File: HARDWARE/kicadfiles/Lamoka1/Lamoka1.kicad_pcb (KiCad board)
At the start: 2 copper layers, 48 parts, among them J1 Boostconverteroutput, J2 Boostconverterinput, J3 Groundconnection, Q1 CSD19531Q5A, Q2 CSD19531Q5A, Q3 CSD19531Q5A, Q4 CSD19531Q5A, U2 LM5122QMHE/NOPB, U3 LM5122QMHE/NOPB

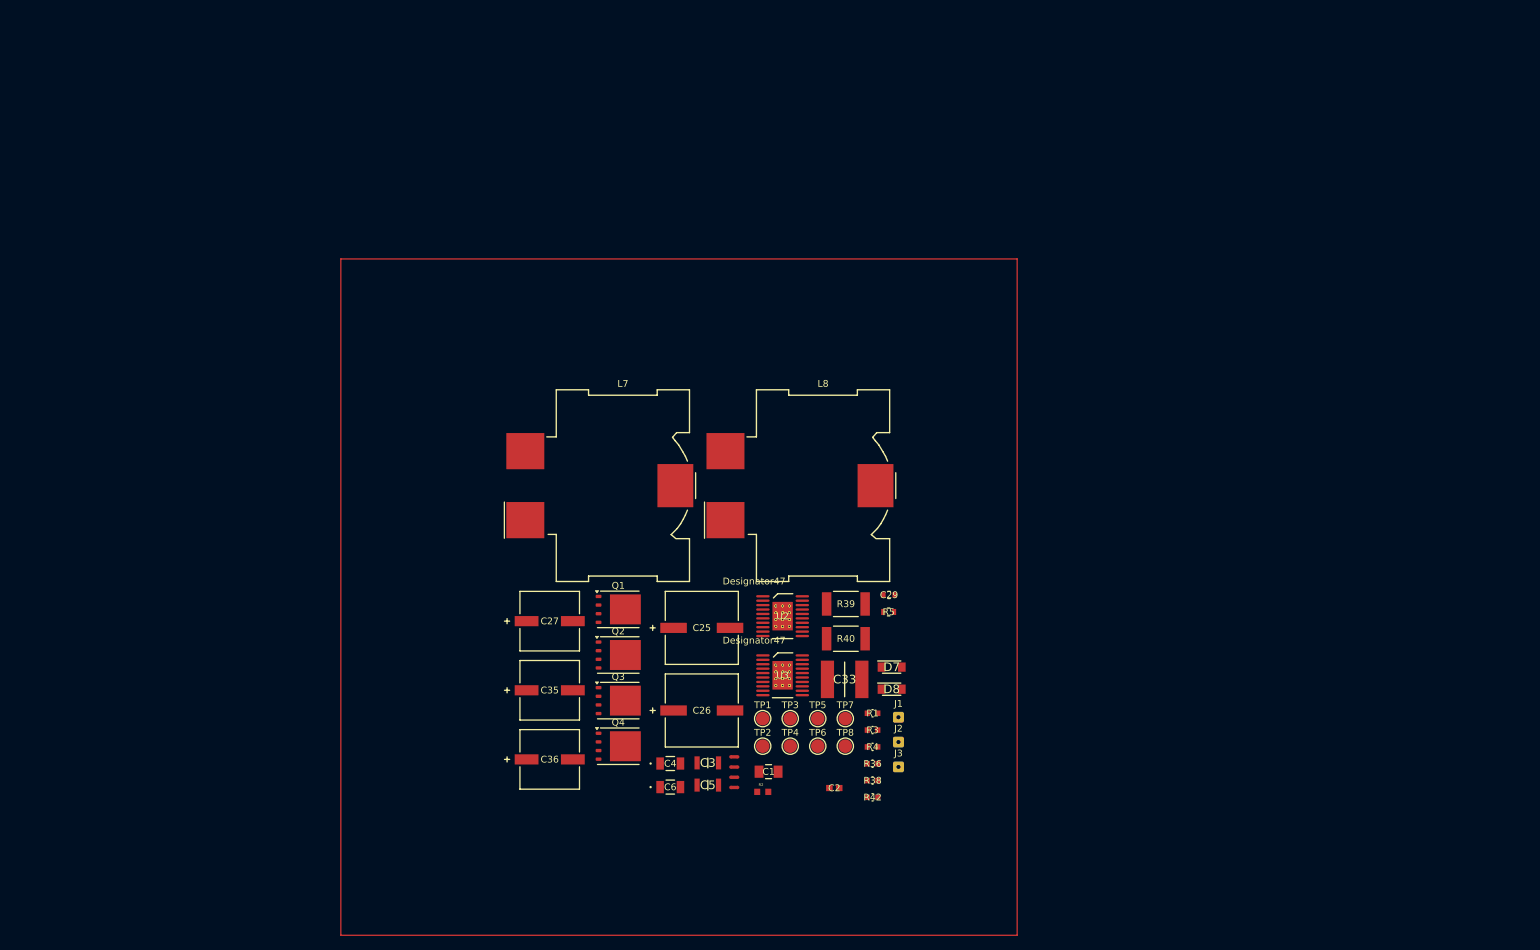
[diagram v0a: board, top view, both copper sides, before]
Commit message: Take things out so boost converter can be standalone
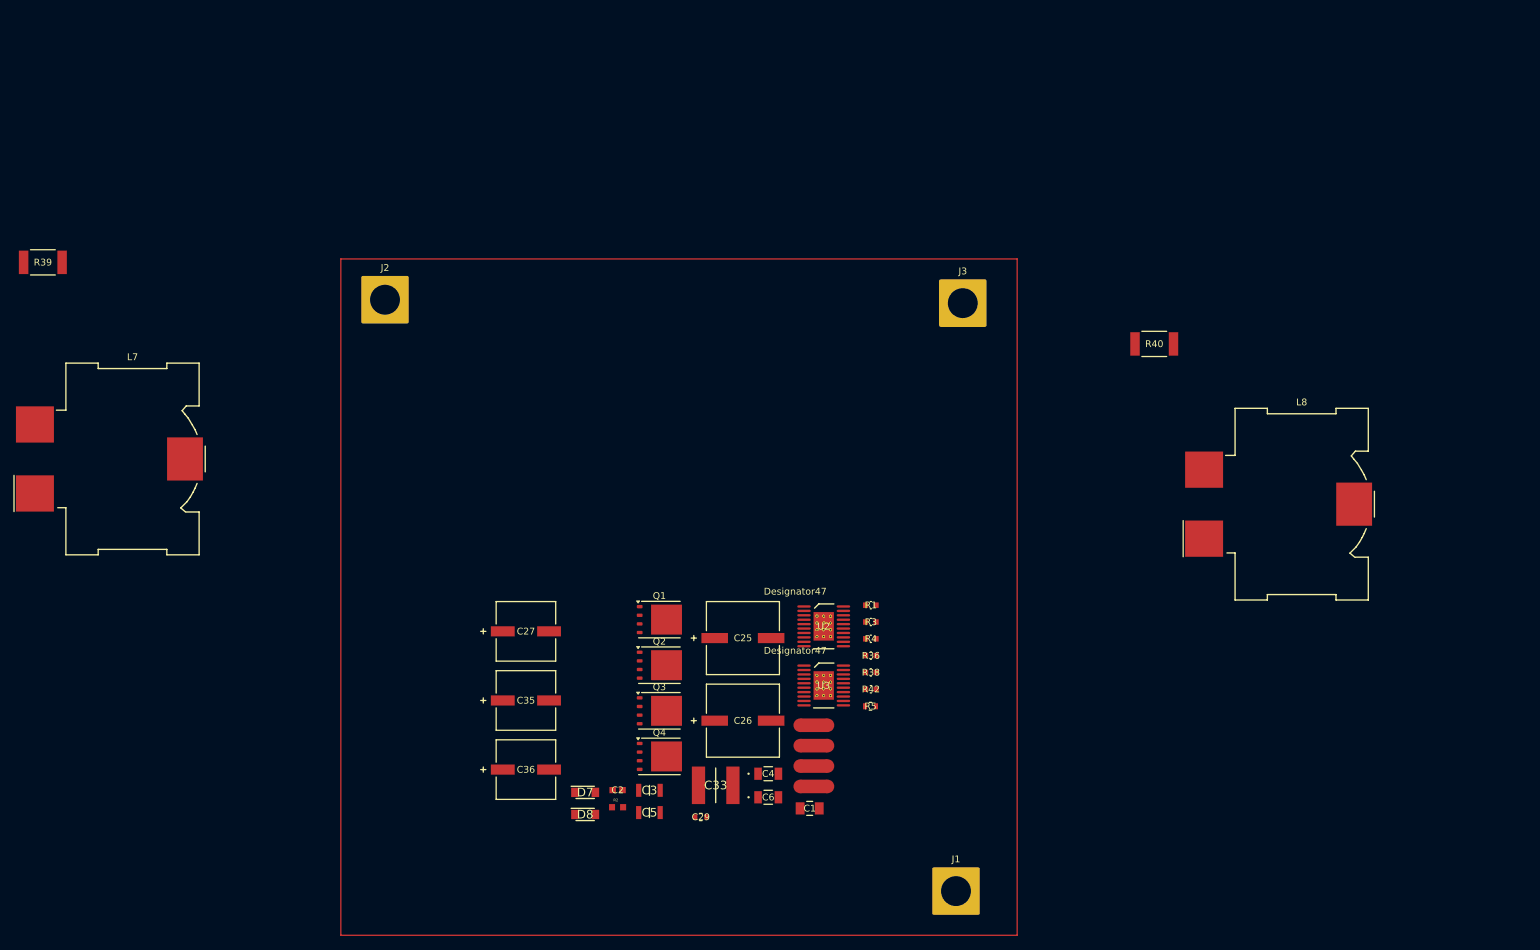
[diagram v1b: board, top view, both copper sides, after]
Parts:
- removed TP1, TP3, TP4, TP5: Tomachie_TP_N, TestPoint:TestPoint_Pad_D2.0mm
- removed TP2: Tomachie_TP_S, TestPoint:TestPoint_Pad_D2.0mm
- removed TP6, TP7, TP8: Tomachie_TP_W, TestPoint:TestPoint_Pad_D2.0mm
- J1, J2, J3: footprint Connector_Wire:SolderWire-0.1sqmm_1x01_D0.4mm_OD1mm -> Connector_Wire:SolderWire-6sqmm_1x01_D3.5mm_OD7mm
- NT1, NT2, NT3, NT4: footprint NetTie:NetTie-2_SMD_Pad0.5mm -> NetTie:NetTie-2_SMD_Pad2.0mm
- moved R39 128.4 mm to (44.2, 51.5)
- moved J2 99.7 mm to (94.5, 57.0)
- moved L7 72.2 mm to (57.4, 80.4)
- moved L8 70.5 mm to (229.4, 87.1)
- moved J3 68.9 mm to (179.5, 57.5)
- moved R40 62.8 mm to (207.7, 63.5)
- moved D7 48.7 mm to (123.9, 129.5)
- moved D8 48.7 mm to (123.9, 132.7)
- moved C29 42.8 mm to (141.0, 133.1)
- moved C2 31.9 mm to (128.7, 129.1)
- moved J1 26.9 mm to (178.5, 144.0)
- moved C33 24.5 mm to (143.2, 128.4)
- moved R2 21.5 mm to (128.7, 131.7)
- moved R1 15.9 mm to (166.0, 101.9)
- moved R36 15.9 mm to (166.0, 109.4)
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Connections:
- NT4 pad 1: /BOOST-SECTION/VIN-SOURCE -> /BOOST-SECTION/MODE
- NT4 pad 2: /BOOST-SECTION/CSPM -> /BOOST-SECTION/VCCM

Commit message: Doing random things with the boost converter
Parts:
- NT2, NT4: footprint NetTie:NetTie-2_SMD_Pad2.0mm -> NetTie:NetTie-2_SMD_Pad0.5mm
- moved Q2 134.7 mm to (246.1, 34.8), turned to -90 degrees
- moved Q4 125.9 mm to (257.2, 94.3), turned to -90 degrees
- moved Q1 122.3 mm to (235.8, 35.0), turned to -90 degrees
- moved Q3 113.9 mm to (246.4, 94.4), turned to -90 degrees
- moved L8 99.1 mm to (146.1, 33.3), turned to -90 degrees
- moved R39 83.5 mm to (120.6, 18.0), turned to 180 degrees
- moved R2 76.1 mm to (116.1, 56.6)
- moved R5 73.5 mm to (123.8, 56.6)
- moved R36 71.5 mm to (99.5, 135.8)
- moved L7 66.5 mm to (103.4, 32.4), turned to -90 degrees
- moved R42 65.0 mm to (109.6, 146.6)
- moved R40 64.7 mm to (160.6, 19.1), turned to 180 degrees
- moved C35 64.4 mm to (177.8, 131.4), turned to 180 degrees
- moved C36 62.7 mm to (177.8, 121.8), turned to 180 degrees
- moved NT1 61.6 mm to (147.8, 58.8)
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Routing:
- net GNDPWR: track 0.00 -> 5.08 mm
- net /BOOST-SECTION/SWS: track 0.00 -> 2.54 mm
- net /BOOST-SECTION/SWM: track 0.00 -> 2.54 mm
